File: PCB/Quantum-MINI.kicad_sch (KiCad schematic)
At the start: 80 parts, among them J1 USB C Connector, J2 JTAG_TC2030, SW1 Boot, SW10 MX_SW_solder, SW11 MX_SW_HS, SW12 MX_SW_solder, SW13 MX_SW_HS, SW14 MX_SW_solder, SW15 MX_SW_HS, SW16 MX_SW_solder, SW17 MX_SW_HS, SW18 MX_SW_HS, SW19 MX_SW_solder, SW2 MX_SW_HS, SW20 MX_SW_solder, SW21 MX_SW_HS, SW22 MX_SW_HS, SW23 MX_SW_solder, SW24 MX_SW_HS, SW25 MX_SW_solder, SW26 MX_SW_solder, SW27 MX_SW_HS, SW28 MX_SW_HS, SW29 MX_SW_solder, SW3 MX_SW_solder, SW30 MX_SW_solder, SW31 MX_SW_HS, SW32 MX_SW_solder, SW33 MX_SW_HS, SW34 MX_SW_HS, SW35 MX_SW_solder, SW36 MX_SW_HS, SW37 MX_SW_solder, SW38 MX_SW_HS, SW39 MX_SW_solder, SW4 MX_SW_HS, SW40 MX_SW_HS, SW41 MX_SW_solder, SW5 MX_SW_solder, SW6 MX_SW_solder, SW7 MX_SW_HS, SW8 MX_SW_solder, SW9 MX_SW_HS, U1 XC6206, U2 USBLC6-2SC6, U3 RP2040, U4 W25Q128JVS, Y1 12MHz

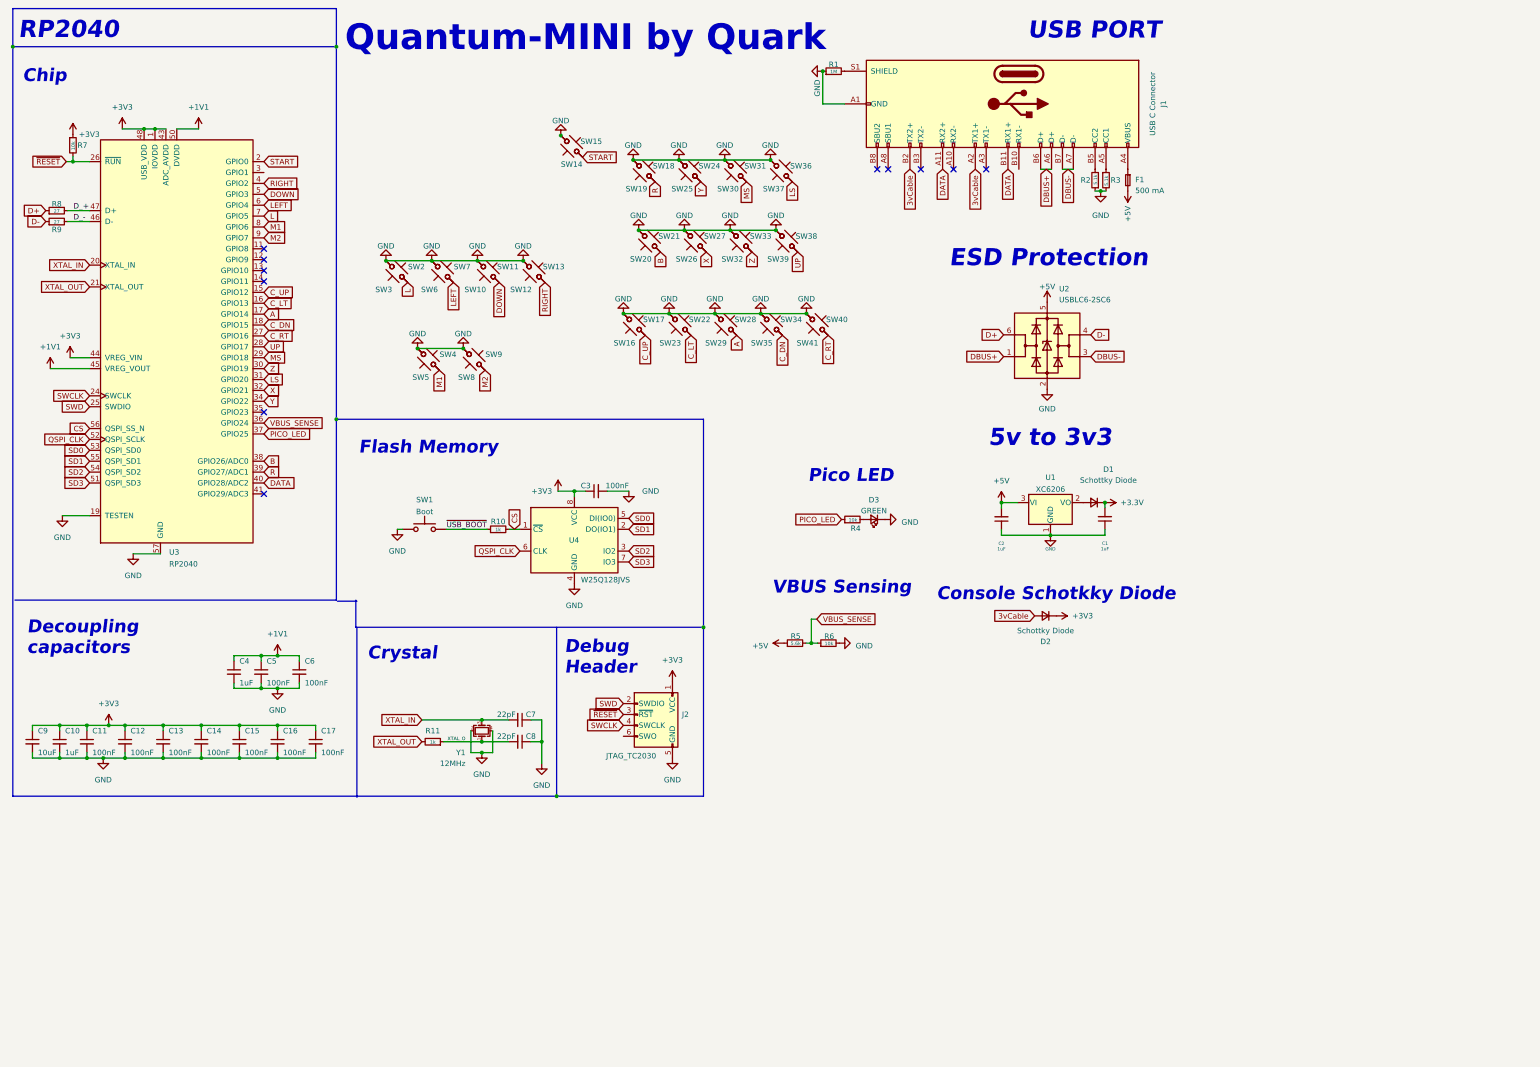
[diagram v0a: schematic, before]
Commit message: Decided to use a daughterboard
- Removed USB port
- Re-arranged rp2040 circuit
- Added USB passthrough
- Adjusted board outline
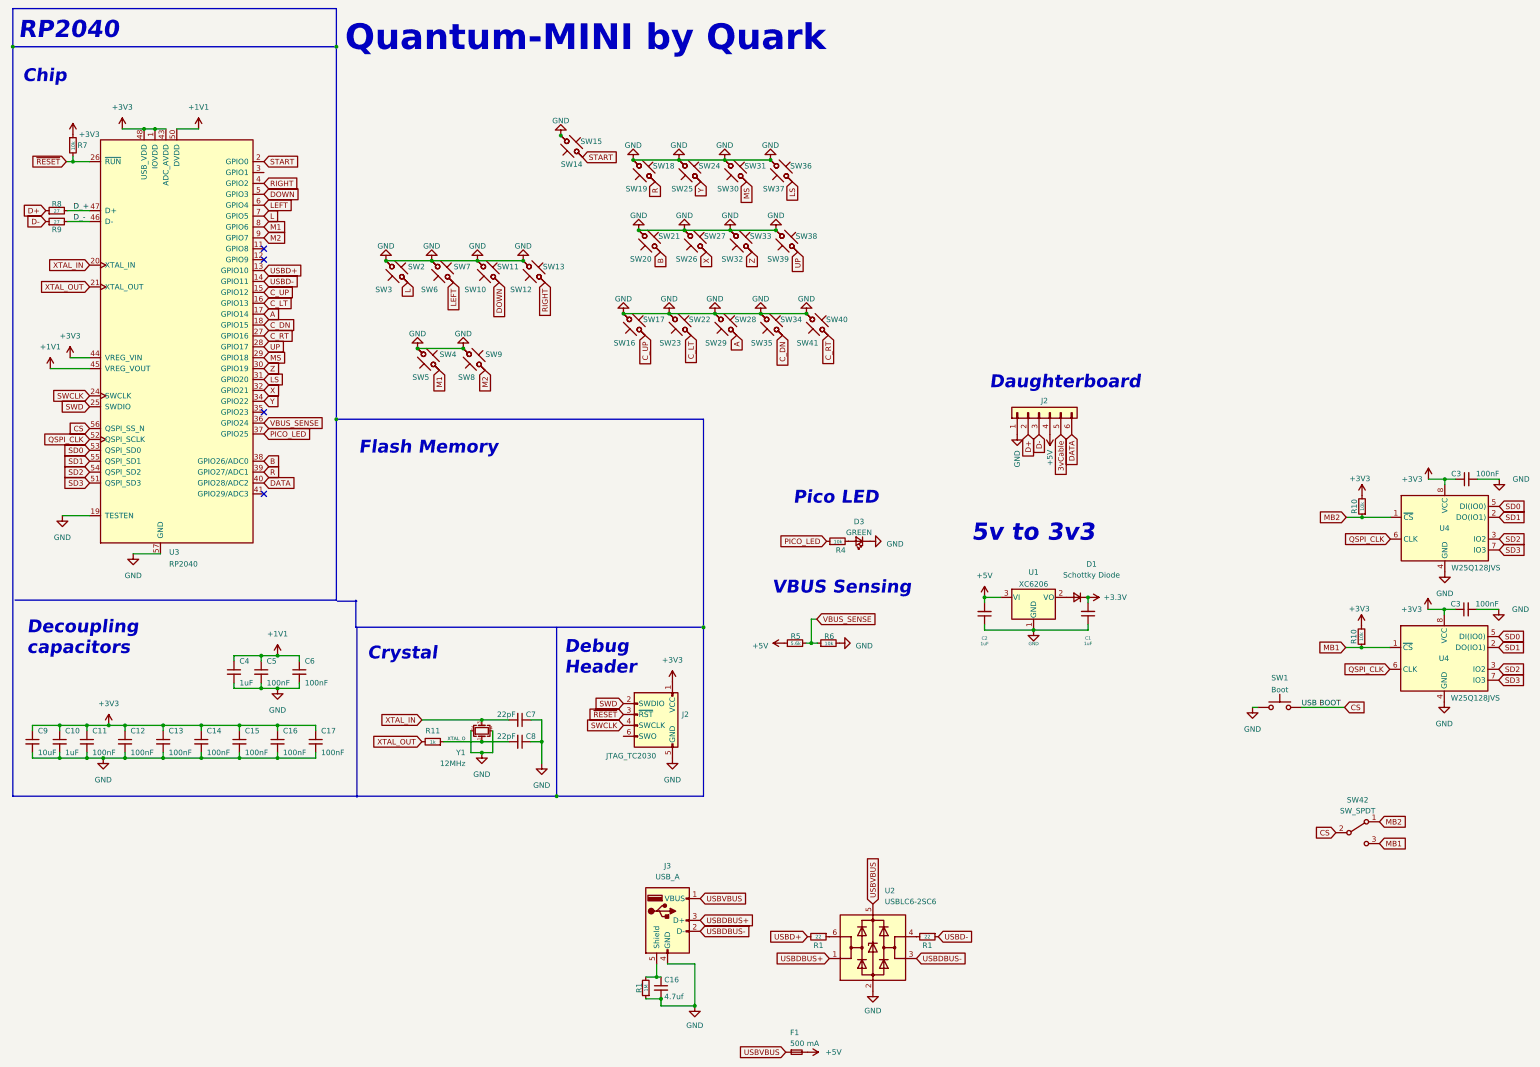
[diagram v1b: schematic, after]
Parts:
- removed D2: Schottky Diode, Diode_SMD:D_SOD-123, symbol Device:D_Small
- removed J1: USB C Connector, footprints:TYPE-C_24P_QCHT, symbol Connector:USB_C_Receptacle
- removed R1: 1M, Resistor_SMD:R_0603_1608Metric, symbol Device:R_Small
- removed R2, R3: 5.1k, Resistor_SMD:R_0402_1005Metric, symbol Device:R_Small
- added C16: 4.7uf, Capacitor_SMD:C_0603_1608Metric, symbol Device:C_Small
- added C3: 100nF, Capacitor_SMD:C_0402_1005Metric, symbol Device:C_Small
- added J2: Conn_01x06, Connector_PinSocket_2.54mm:PinSocket_1x06_P2.54mm_Horizontal, symbol Connector_Generic:Conn_01x06
- added J3: USB_A, USB1130-15-A:GCT_USB1130-15-A_REVA, symbol Connector:USB_A
- added R1: 1M, Resistor_SMD:R_0603_1608Metric, symbol Device:R_Small
- added R1 (x2): 22, Resistor_SMD:R_0603_1608Metric, symbol Device:R_Small
- added R10: 10k, Resistor_SMD:R_0402_1005Metric, symbol Device:R_Small
- added SW42: SW_SPDT, Button_Switch_SMD:SW_SPDT_PCM12, symbol Switch:SW_SPDT
- added U4: W25Q128JVS, Package_SO:SOIC-8_5.23x5.23mm_P1.27mm, symbol Memory_Flash:W25Q128JVS
- R10: value 1k -> 10k
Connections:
- net +3V3: now also R10.2, C3.1, R10.2, U4.8 (VCC)
- net +5V: now also J2.4 (Pin_4); no longer U2.5 (VBUS)
- net 3vCable: now also J2.5 (Pin_5)
- net CS: now also SW1.2, SW42.2 (B); no longer R10.2, U4.1 (~{CS})
- net D+: now also J2.2 (Pin_2); no longer U2.6 (I/O1)
- net D-: now also J2.3 (Pin_3); no longer U2.4 (I/O2)
- net DATA: now also J2.6 (Pin_6)
- net GND: now also C16.2, C3.2, J2.1 (Pin_1), J3.4 (GND), R1.1, U4.4 (GND)
- net QSPI_CLK: now also U4.6 (CLK)
- net SD0: now also U4.5 (DI(IO0))
- net SD1: now also U4.2 (DO(IO1))
- net SD2: now also U4.3 (IO2)
- net SD3: now also U4.7 (IO3)
- net USBVBUS: now reaches F1.1
- net USBVBUS: now also U2.5 (VBUS), J3.1 (VBUS)
- net USBD+: now reaches U3.13 (GPIO10)
- net USBD+: now also R1.2
- net USBD-: now reaches U3.14 (GPIO11)
- net USBD-: now also R1.1
- net DBUS+ renamed USBDBUS+
- net USBDBUS+: now also J3.3 (D+)
- net DBUS- renamed USBDBUS-
- net USBDBUS-: now also J3.2 (D-)
- net ~{USB_BOOT} renamed MB1
- net MB1: now also U4.1 (~{CS}), SW42.3 (C); no longer SW1.2
- new net: C16.1, J3.5 (Shield), R1.2
- new net: R1.1, U2.6 (I/O1)
- new net: R1.2, U2.4 (I/O2)
- new net MB2: R10.1, SW42.1 (A), U4.1 (~{CS})
- no-connect marks 11 -> 4
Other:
- note added: "Daughterboard"
- note removed: "Console Schotkky Diode"
- note removed: "ESD Protection"
- note removed: "USB PORT"
- moved on the sheet: C1, C2, C3, D1, D3, R10, R4, SW1, U1, U4
